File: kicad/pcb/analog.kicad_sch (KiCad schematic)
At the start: 20 parts, among them U2 74HC4051, U5 OPA354AIDBVR

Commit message: rerouted pcb
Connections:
- net COL0: now also R8.1, U2.13 (A0); no longer R11.1, U2.12 (A3)
- net COL1: now also R9.1, U2.14 (A1); no longer R8.1, U2.13 (A0)
- net COL2: now also R10.1, U2.15 (A2); no longer R9.1, U2.14 (A1)
- net COL3: now also R11.1, U2.12 (A3); no longer R10.1, U2.15 (A2)
- net COL5: now also R8.1, U2.15 (A2); no longer R11.1, U2.1 (A4)
- net COL6: now also R9.1, U2.1 (A4); no longer R11.1, U2.12 (A3)
- net COL7: now also R11.1, U2.2 (A6); no longer R8.1, U2.13 (A0)
- net COL8: now also R11.1, U2.4 (A7); no longer R9.1, U2.14 (A1)
- net COL9: now also U2.5 (A5); no longer U2.15 (A2)
- net GND: now also U2.12 (A3), U2.13 (A0), U2.14 (A1); no longer U2.2 (A6), U2.4 (A7), U2.5 (A5)
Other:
- moved on the sheet: R10, R11, R8, R9

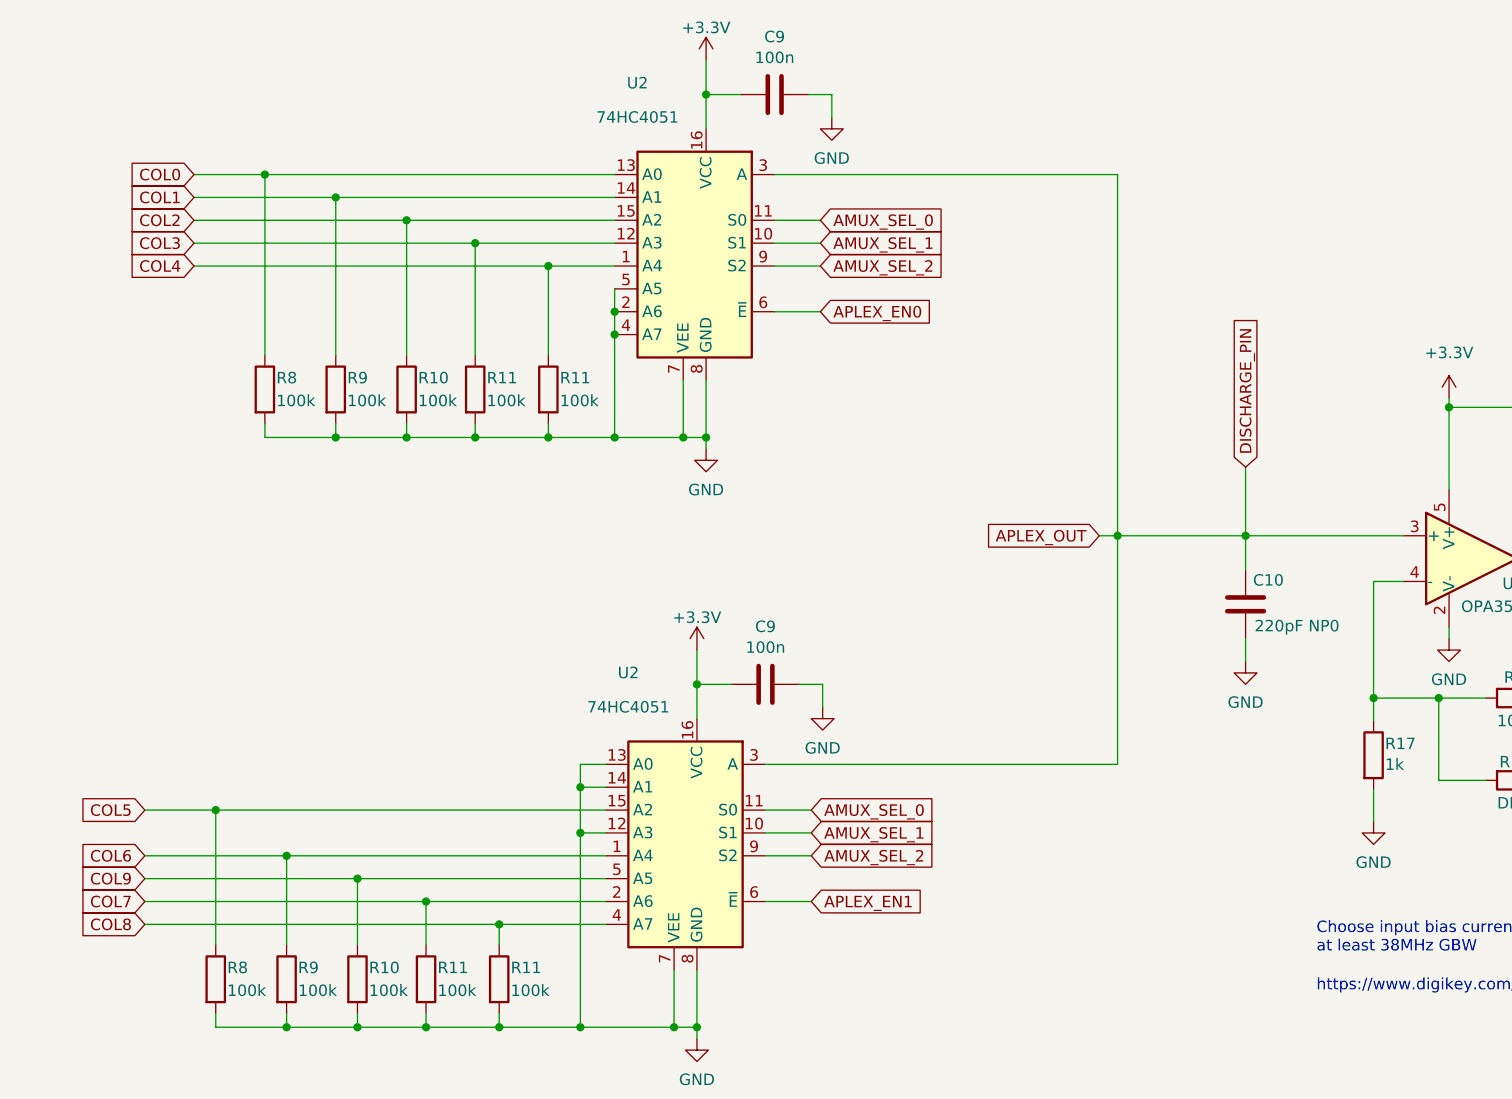
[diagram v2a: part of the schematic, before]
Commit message: Major fixes after prototype order
Fixed the following:
- wrong RGB schematic, D106-D111 doesn't work
- discharge pin from analog circuit was not connected
- plate holes had the wrong diameter
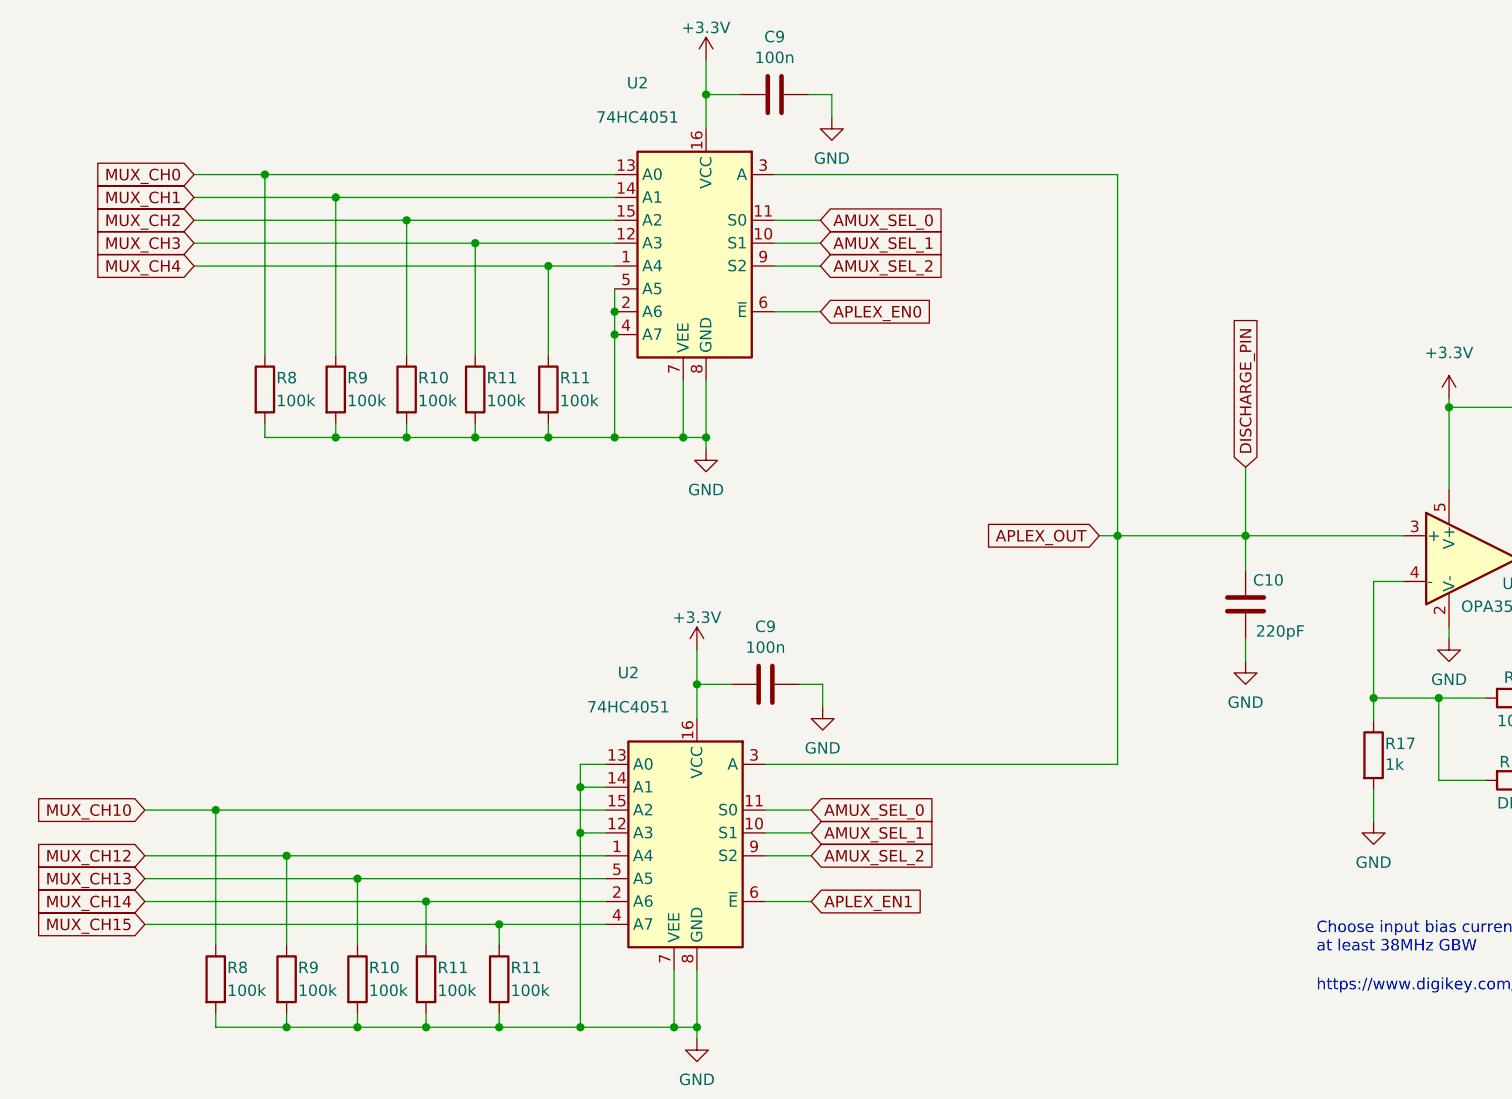
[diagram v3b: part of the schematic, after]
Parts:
- C10: value 220pF NP0 -> 220pF
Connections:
- net COL0 renamed MUX_CH0
- net COL1 renamed MUX_CH1
- net COL2 renamed MUX_CH2
- net COL3 renamed MUX_CH3
- net COL4 renamed MUX_CH4
- net COL5 renamed MUX_CH10
- net COL6 renamed MUX_CH12
- net COL7 renamed MUX_CH14
- net COL8 renamed MUX_CH15
- net COL9 renamed MUX_CH13
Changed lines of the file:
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@@
   (title_block
     (title "Le Capybara")
-    (date "2023-08-22")
-    (rev "0.1")
+    (date "2023-09-01")
+    (rev "0.2")
     (company "sporkus")
   )
@@
     )
   )
-  (global_label "COL5" (shape input) (at 42.799 112.522 180) (fields_autoplaced)
+  (global_label "MUX_CH14" (shape input) (at 42.799 122.682 180) (fields_autoplaced)
     (effects (font (size 1.27 1.27)) (justify right))
-    (property "Intersheetrefs" "${INTERSHEET_REFS}" (at 35.0551 112.522 0)
+    (property "Intersheetrefs" "${INTERSHEET_REFS}" (at 29.9147 122.682 0)
       (effects (font (size 1.27 1.27)) (justify right) hide)
     )
@@
     )
   )
-  (global_label "COL6" (shape input) (at 42.799 117.602 180) (fields_autoplaced)
+  (global_label "MUX_CH3" (shape input) (at 48.26 49.53 180) (fields_autoplaced)
     (effects (font (size 1.27 1.27)) (justify right))
-    (property "Intersheetrefs" "${INTERSHEET_REFS}" (at 35.0551 117.602 0)
+    (property "Intersheetrefs" "${INTERSHEET_REFS}" (at 36.5852 49.53 0)
       (effects (font (size 1.27 1.27)) (justify right) hide)
     )
   )
-  (global_label "COL0" (shape input) (at 48.26 41.91 180) (fields_autoplaced)
+  (global_label "MUX_CH12" (shape input) (at 42.799 117.602 180) (fields_autoplaced)
     (effects (font (size 1.27 1.27)) (justify right))
-    (property "Intersheetrefs" "${INTERSHEET_REFS}" (at 26.67 -102.87 0)
-      (effects (font (size 1.27 1.27)) hide)
+    (property "Intersheetrefs" "${INTERSHEET_REFS}" (at 29.9147 117.602 0)
+      (effects (font (size 1.27 1.27)) (justify right) hide)
     )
   )
@@
     )
   )
-  (global_label "COL7" (shape input) (at 42.799 122.682 180) (fields_autoplaced)
-    (effects (font (size 1.27 1.27)) (justify right))
-    (property "Intersheetrefs" "${INTERSHEET_REFS}" (at 35.5478 122.6026 0)
-      (effects (font (size 1.27 1.27)) (justify right) hide)
-    )
-  )
-  (global_label "COL8" (shape input) (at 42.799 125.222 180) (fields_autoplaced)
-    (effects (font (size 1.27 1.27)) (justify right))
-    (property "Intersheetrefs" "${INTERSHEET_REFS}" (at 35.0551 125.222 0)
-      (effects (font (size 1.27 1.27)) (justify right) hide)
-    )
-  )
   (global_label "APLEX_EN0" (shape input) (at 117.856 57.15 0) (fields_autoplaced)
     (effects (font (size 1.27 1.27)) (justify left))
@@
     )
   )
-  (global_label "COL2" (shape input) (at 48.26 46.99 180) (fields_autoplaced)
+  (global_label "MUX_CH15" (shape input) (at 42.799 125.222 180) (fields_autoplaced)
     (effects (font (size 1.27 1.27)) (justify right))
-    (property "Intersheetrefs" "${INTERSHEET_REFS}" (at 26.67 -90.17 0)
-      (effects (font (size 1.27 1.27)) hide)
-    )
-  )
-  (global_label "COL1" (shape input) (at 48.26 44.45 180) (fields_autoplaced)
+    (property "Intersheetrefs" "${INTERSHEET_REFS}" (at 29.9147 125.222 0)
+      (effects (font (size 1.27 1.27)) (justify right) hide)
+    )
+  )
+  (global_label "MUX_CH13" (shape input) (at 42.799 120.142 180) (fields_autoplaced)
     (effects (font (size 1.27 1.27)) (justify right))
-    (property "Intersheetrefs" "${INTERSHEET_REFS}" (at 26.67 -95.25 0)
-      (effects (font (size 1.27 1.27)) hide)
+    (property "Intersheetrefs" "${INTERSHEET_REFS}" (at 29.9147 120.142 0)
+      (effects (font (size 1.27 1.27)) (justify right) hide)
     )
   )
@@
     )
   )
-  (global_label "COL9" (shape input) (at 42.799 120.142 180) (fields_autoplaced)
-    (effects (font (size 1.27 1.27)) (justify right))
-    (property "Intersheetrefs" "${INTERSHEET_REFS}" (at 35.0551 120.142 0)
-      (effects (font (size 1.27 1.27)) (justify right) hide)
-    )
-  )
   (global_label "APLEX_EN1" (shape input) (at 116.84 122.682 0) (fields_autoplaced)
     (effects (font (size 1.27 1.27)) (justify left))
@@
     )
   )
+  (global_label "MUX_CH4" (shape input) (at 48.26 52.07 180) (fields_autoplaced)
+    (effects (font (size 1.27 1.27)) (justify right))
+    (property "Intersheetrefs" "${INTERSHEET_REFS}" (at 36.5852 52.07 0)
+      (effects (font (size 1.27 1.27)) (justify right) hide)
+    )
+  )
+  (global_label "MUX_CH10" (shape input) (at 42.799 112.522 180) (fields_autoplaced)
+    (effects (font (size 1.27 1.27)) (justify right))
+    (property "Intersheetrefs" "${INTERSHEET_REFS}" (at 29.9147 112.522 0)
+      (effects (font (size 1.27 1.27)) (justify right) hide)
+    )
+  )
   (global_label "AMUX_SEL_0" (shape input) (at 116.84 112.522 0) (fields_autoplaced)
     (effects (font (size 1.27 1.27)) (justify left))
@@
     )
   )
-  (global_label "COL3" (shape input) (at 48.26 49.53 180) (fields_autoplaced)
+  (global_label "MUX_CH1" (shape input) (at 48.26 44.45 180) (fields_autoplaced)
     (effects (font (size 1.27 1.27)) (justify right))
-    (property "Intersheetrefs" "${INTERSHEET_REFS}" (at 26.67 -80.01 0)
-      (effects (font (size 1.27 1.27)) hide)
+    (property "Intersheetrefs" "${INTERSHEET_REFS}" (at 36.5852 44.45 0)
+      (effects (font (size 1.27 1.27)) (justify right) hide)
     )
   )
@@
     )
   )
-  (global_label "COL4" (shape input) (at 48.26 52.07 180) (fields_autoplaced)
+  (global_label "MUX_CH2" (shape input) (at 48.26 46.99 180) (fields_autoplaced)
     (effects (font (size 1.27 1.27)) (justify right))
-    (property "Intersheetrefs" "${INTERSHEET_REFS}" (at 26.67 -80.01 0)
-      (effects (font (size 1.27 1.27)) hide)
+    (property "Intersheetrefs" "${INTERSHEET_REFS}" (at 36.5852 46.99 0)
+      (effects (font (size 1.27 1.27)) (justify right) hide)
+    )
+  )
+  (global_label "MUX_CH0" (shape input) (at 48.26 41.91 180) (fields_autoplaced)
+    (effects (font (size 1.27 1.27)) (justify right))
+    (property "Intersheetrefs" "${INTERSHEET_REFS}" (at 36.5852 41.91 0)
+      (effects (font (size 1.27 1.27)) (justify right) hide)
     )
   )
@@
       (effects (font (size 1.27 1.27)))
     )
-    (property "Value" "220pF NP0" (at 170.815 92.075 0)
-      (effects (font (size 1.27 1.27)))
-    )
+    (property "Value" "220pF" (at 168.9534 92.6652 0)
+      (effects (font (size 1.27 1.27)))
+    )
